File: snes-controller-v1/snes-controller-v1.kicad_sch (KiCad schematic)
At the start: 19 parts, among them J2 NES, J3 Conn_01x06, J3 USB_B_Micro, U1 ATSAMD21E18A-A, U1 SN74LVC125ADR, U2 AP2112K-3.3

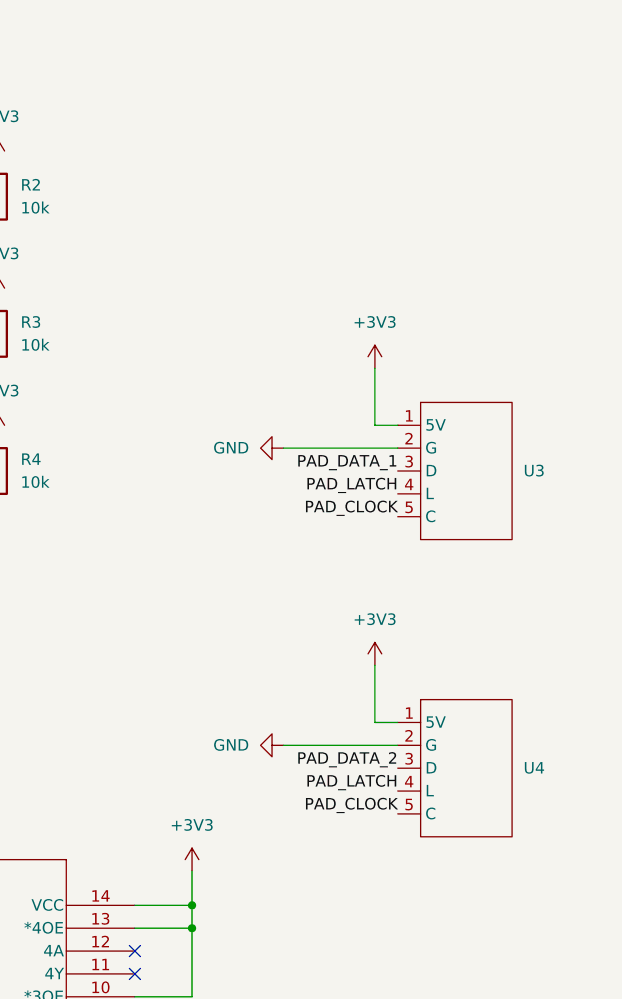
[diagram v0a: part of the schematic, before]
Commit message: update controller port
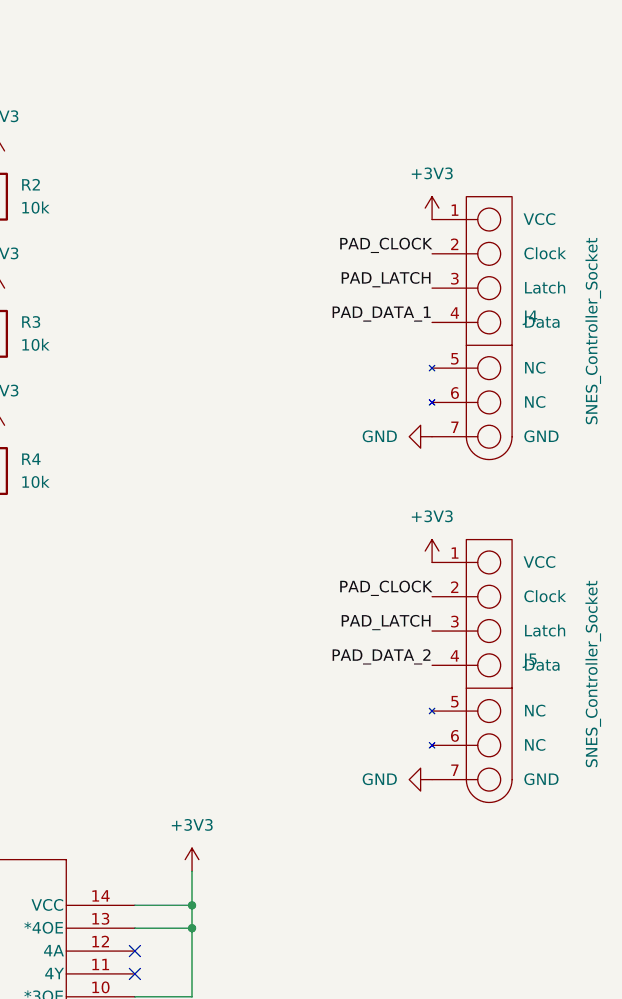
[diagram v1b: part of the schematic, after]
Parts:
- removed U3, U4: ~, Minor_Industries:NES controller port, symbol Minor_Industries:Nes_Controller_Port
- added J4, J5: SNES_Controller_Socket, Nintendo:SNES_Controller_Socket, symbol Minor_Industries:SNES_Controller_Socket
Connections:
- net +3V3: now also J4.1 (VCC), J5.1 (VCC)
- net GND: now also J4.7 (GND), J5.7 (GND)
- net PAD_CLOCK: now also J4.2 (Clock), J5.2 (Clock)
- net PAD_DATA_1: now also J4.4 (Data)
- net PAD_DATA_2: now also J5.4 (Data)
- net PAD_LATCH: now also J4.3 (Latch), J5.3 (Latch)

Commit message: update socket on PCB
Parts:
- J4, J5: footprint Nintendo:SNES_Controller_Socket -> Minor_Industries:SNES_Controller_Socket
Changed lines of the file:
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@@
       (effects (font (size 1.27 1.27)) (justify left))
     )
-    (property "Footprint" "Nintendo:SNES_Controller_Socket" (at 251.46 53.34 0)
+    (property "Footprint" "Minor_Industries:SNES_Controller_Socket" (at 251.46 53.34 0)
       (effects (font (size 1.27 1.27)) hide)
     )
@@
       (effects (font (size 1.27 1.27)) (justify left))
     )
-    (property "Footprint" "Nintendo:SNES_Controller_Socket" (at 251.46 91.44 0)
-      (effects (font (size 1.27 1.27)) hide)
-    )
+    (property "Footprint" "Minor_Industries:SNES_Controller_Socket" (at 251.46 91.44 0)
+      (effects (font (size 1.27 1.27)) hide)
+    )

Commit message: ground plane
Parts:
- removed C8: 1uF, Capacitor_SMD:C_0805_2012Metric, symbol Device:C
- J3: value Conn_01x06 -> Conn_01x05; footprint Connector_PinSocket_2.54mm:PinSocket_1x06_P2.54mm_Vertical -> Connector_PinSocket_2.54mm:PinSocket_1x05_P2.54mm_Vertical; symbol Connector_Generic:Conn_01x06 -> Connector_Generic:Conn_01x05
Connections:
- no-connect marks 22 -> 21
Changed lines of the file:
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@@
   (junction (at 62.23 157.48) (diameter 0) (color 0 0 0 0)
   )
-  (junction (at 74.93 157.48) (diameter 0) (color 0 0 0 0)
-  )
   (junction (at 35.56 134.62) (diameter 0) (color 0 0 0 0)
   )
@@
   (junction (at 229.87 120.65) (diameter 0) (color 0 0 0 0)
   )
-  (junction (at 74.93 134.62) (diameter 0) (color 0 0 0 0)
-  )
   (junction (at 45.72 157.48) (diameter 0) (color 0 0 0 0)
   )
@@
   )
   (no_connect (at 40.64 86.36))
-  (no_connect (at 143.51 180.34))
   (no_connect (at 96.52 88.9))
   (no_connect (at 96.52 99.06))
@@
     (stroke (width 0) (type default))
   )
-  (wire (pts (xy 86.36 157.48) (xy 74.93 157.48))
-    (stroke (width 0) (type default))
-  )
   (wire (pts (xy 165.1 97.79) (xy 176.53 97.79))
     (stroke (width 0) (type default))
@@
     (stroke (width 0) (type default))
   )
-  (wire (pts (xy 86.36 148.59) (xy 86.36 157.48))
-    (stroke (width 0) (type default))
-  )
   (wire (pts (xy 62.23 148.59) (xy 62.23 157.48))
     (stroke (width 0) (type default))
@@
     (stroke (width 0) (type default))
   )
-  (wire (pts (xy 74.93 134.62) (xy 86.36 134.62))
-    (stroke (width 0) (type default))
-  )
   (wire (pts (xy 96.52 20.32) (xy 106.68 20.32))
     (stroke (width 0) (type default))
@@
   )
   (wire (pts (xy 88.9 121.92) (xy 96.52 121.92))
-    (stroke (width 0) (type default))
-  )
-  (wire (pts (xy 86.36 134.62) (xy 86.36 140.97))
     (stroke (width 0) (type default))
   )
@@
     )
   )
-  (symbol (lib_id "Connector_Generic:Conn_01x06") (at 148.59 172.72 0) (unit 1)
-    (in_bom yes) (on_board yes) (dnp no) (fields_autoplaced)
-    (property "Reference" "J3" (at 151.13 172.72 0)
-      (effects (font (size 1.27 1.27)) (justify left))
-    )
-    (property "Value" "Conn_01x06" (at 151.13 175.26 0)
-      (effects (font (size 1.27 1.27)) (justify left))
-    )
-    (property "Footprint" "Connector_PinSocket_2.54mm:PinSocket_1x06_P2.54mm_Vertical" (at 148.59 172.72 0)
+  (symbol (lib_id "Connector_Generic:Conn_01x05") (at 148.59 172.72 0) (unit 1)
+    (in_bom yes) (on_board yes) (dnp no)
+    (property "Reference" "J3" (at 148.59 165.1 0)
+      (effects (font (size 1.27 1.27)))
+    )
+    (property "Value" "Conn_01x05" (at 148.59 180.34 0)
+      (effects (font (size 1.27 1.27)))
+    )
+    (property "Footprint" "Connector_PinSocket_2.54mm:PinSocket_1x05_P2.54mm_Vertical" (at 148.59 172.72 0)
       (effects (font (size 1.27 1.27)) hide)
     )
@@
     (pin "4")
     (pin "5")
-    (pin "6")
     (instances
       (project "snes-controller-v1"
@@
         )
       )
-    )
-  )
-  (symbol (lib_id "Device:C") (at 86.36 144.78 0) (unit 1)
-    (in_bom yes) (on_board yes) (dnp no) (fields_autoplaced)
-    (property "Reference" "C8" (at 90.17 143.51 0)
-      (effects (font (size 1.27 1.27)) (justify left))
-    )
-    (property "Value" "1uF" (at 90.17 146.05 0)
-      (effects (font (size 1.27 1.27)) (justify left))
-    )
-    (property "Footprint" "Capacitor_SMD:C_0805_2012Metric" (at 87.3252 148.59 0)
-      (effects (font (size 1.27 1.27)) hide)
-    )
-    (property "Datasheet" "~" (at 86.36 144.78 0)
-      (effects (font (size 1.27 1.27)) hide)
-    )
-    (pin "1")
-    (pin "2")
-    (instances
-      (project "snes-controller-v1"
-        (path "/eb34aa8d-b454-4de7-98a6-8535b6a0e862"
-          (reference "C8") (unit 1)
-        )
-      )
